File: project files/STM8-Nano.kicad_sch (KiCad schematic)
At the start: 29 parts, among them J1 RIGHT, J2 LEFT, J3 USB_C_Receptacle, J4 SWIM, SW1 RESET, SW2 VCC, U1 STM8F105K4, U2 CH340E, Y1 16MHZ

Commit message: added annotation
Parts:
- removed C7: 1uF, Capacitor_SMD:C_0603_1608Metric, symbol Device:C
- removed C8: 100nF, Capacitor_SMD:C_0603_1608Metric, symbol Device:C
- removed J3: USB_C_Receptacle, Connector_USB:USB_C_Receptacle_Palconn_UTC16-G, symbol Connector:USB_C_Receptacle
- removed L1: L, symbol Device:L
- added C9: 10uF, Capacitor_SMD:C_0603_1608Metric, symbol Device:C
- added J3: USB_C_Receptacle_USB2.0, Connector_USB:USB_C_Receptacle_Palconn_UTC16-G, symbol Connector:USB_C_Receptacle_USB2.0
- D2: value TX -> TX↓
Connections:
- net VDDA is gone; now on net VCC: U1.7 (VDDIO)
- net +5V: now also U2.7 (VCC)
- net GND: now also J4.3 (Pin_3), J3.A1 (GND), J3.A12 (GND), J3.B1 (GND), J3.B12 (GND); no longer J4.4 (Pin_4)
- net USB(+): now also J3.A6 (D+), J3.B6 (D+)
- net USB(-): now also J3.A7 (D-), J3.B7 (D-)
- net VCC: no longer U2.7 (VCC)
- net ~{RST}: now also J4.4 (Pin_4), C9.2; no longer J4.3 (Pin_3)
- net at R1.1: now also J3.B5 (CC2)
- net at R2.1: now also J3.A5 (CC1)
- net at U2.4 (~{RTS}): now also C9.1
- new net: J3.A4 (VBUS), J3.A9 (VBUS), J3.B4 (VBUS), J3.B9 (VBUS)
- no-connect marks 14 -> 5
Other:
- note added: "Arduino Nano pin functions: D1 | TX D0 | RX Reset GND D2 | Interrupt ~D3 | Interrupt D4 ~D5 ~D6 D7 D8 ~D9 ~D10 | SS ~D11 | MOSI ~D12 | MISO"
- note added: "Arduino Nano pin functions: Vin GND Reset +5V A7 | D21 A6 | D20 A5 | D19 | SCL A4 | D18 | SDA A3 | D17 A2 | D16 A1 | D15 A0 | D14 Aref +3.3V D13 | SCK"
- moved on the sheet: C3, C4, D1, D2, J1, J2, R3, R4, U2

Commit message: case change
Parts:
- removed R7: 0R, Resistor_SMD:R_0805_2012Metric, symbol Device:R
- C1, C3, C4, C5, C6, C9: footprint Capacitor_SMD:C_0603_1608Metric -> Capacitor_SMD:C_0402_1005Metric
- D1, D2, D3, D4: footprint LED_SMD:LED_0603_1608Metric -> LED_SMD:LED_0402_1005Metric
- R1, R2, R3, R4, R5, R6: footprint Resistor_SMD:R_0603_1608Metric_Pad0.98x0.95mm_HandSolder -> Resistor_SMD:R_0402_1005Metric

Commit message: up
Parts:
- SW2: footprint Jumper:SolderJumper-3_P2.0mm_Open_TrianglePad1.0x1.5mm_NumberLabels -> Button_Switch_SMD:SW_SPDT_PCM12
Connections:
- net VBUS: now reaches J3.A4 (VBUS), J3.A9 (VBUS), J3.B4 (VBUS), J3.B9 (VBUS)
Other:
- moved on the sheet: SW2
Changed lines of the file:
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@@
     (stroke (width 0) (type default) (color 0 0 0 0))
   )
-  (wire (pts (xy 17.78 123.19) (xy 17.78 120.65))
+  (wire (pts (xy 251.46 63.5) (xy 251.46 60.96))
     (stroke (width 0) (type default) (color 0 0 0 0))
   )
@@
     (stroke (width 0) (type default) (color 0 0 0 0))
   )
-  (wire (pts (xy 20.32 123.19) (xy 17.78 123.19))
+  (wire (pts (xy 254 63.5) (xy 251.46 63.5))
     (stroke (width 0) (type default) (color 0 0 0 0))
   )
@@
     (stroke (width 0) (type default) (color 0 0 0 0))
   )
-  (wire (pts (xy 38.1 125.73) (xy 38.1 120.65))
-    (stroke (width 0) (type default) (color 0 0 0 0))
-  )
-  (wire (pts (xy 30.48 120.65) (xy 33.02 120.65))
+  (wire (pts (xy 271.78 66.04) (xy 271.78 60.96))
+    (stroke (width 0) (type default) (color 0 0 0 0))
+  )
+  (wire (pts (xy 264.16 60.96) (xy 266.7 60.96))
     (stroke (width 0) (type default) (color 0 0 0 0))
   )
@@
     (stroke (width 0) (type default) (color 0 0 0 0))
   )
+  (wire (pts (xy 50.8 35.56) (xy 50.8 33.02))
+    (stroke (width 0) (type default) (color 0 0 0 0))
+  )
   (wire (pts (xy 154.94 54.61) (xy 160.02 54.61))
     (stroke (width 0) (type default) (color 0 0 0 0))
@@
     (stroke (width 0) (type default) (color 0 0 0 0))
   )
-  (wire (pts (xy 30.48 125.73) (xy 38.1 125.73))
+  (wire (pts (xy 264.16 66.04) (xy 271.78 66.04))
     (stroke (width 0) (type default) (color 0 0 0 0))
   )
@@
   )
   (wire (pts (xy 85.09 35.56) (xy 85.09 38.1))
+    (stroke (width 0) (type default) (color 0 0 0 0))
+  )
+  (wire (pts (xy 48.26 35.56) (xy 50.8 35.56))
     (stroke (width 0) (type default) (color 0 0 0 0))
   )
@@
   )
   (label "D1{slash}TX" (at 114.3 45.72 180)
+    (effects (font (size 1.27 1.27)) (justify right bottom))
+  )
+  (label "VIN" (at 55.88 142.24 180)
     (effects (font (size 1.27 1.27)) (justify right bottom))
   )
@@
     (pin "1")
     (pin "2")
+  )
+  (symbol (lib_id "power:+3.3V") (at 96.52 135.89 0) (unit 1)
+    (in_bom yes) (on_board yes) (fields_autoplaced)
+    (property "Reference" "#PWR0110" (id 0) (at 96.52 139.7 0)
+      (effects (font (size 1.27 1.27)) hide)
+    )
+    (property "Value" "+3.3V" (id 1) (at 96.52 130.81 0))
+    (property "Footprint" "" (id 2) (at 96.52 135.89 0)
+      (effects (font (size 1.27 1.27)) hide)
+    )
+    (property "Datasheet" "" (id 3) (at 96.52 135.89 0)
+      (effects (font (size 1.27 1.27)) hide)
+    )
+    (pin "1")
   )
   (symbol (lib_id "Connector_Generic:Conn_01x04") (at 274.32 29.21 0) (unit 1)
@@
     (pin "2")
   )
-  (symbol (lib_id "power:VCC") (at 17.78 120.65 0) (unit 1)
-    (in_bom yes) (on_board yes) (fields_autoplaced)
-    (property "Reference" "#PWR01" (id 0) (at 17.78 124.46 0)
-      (effects (font (size 1.27 1.27)) hide)
-    )
-    (property "Value" "VCC" (id 1) (at 17.78 115.57 0))
-    (property "Footprint" "" (id 2) (at 17.78 120.65 0)
-      (effects (font (size 1.27 1.27)) hide)
-    )
-    (property "Datasheet" "" (id 3) (at 17.78 120.65 0)
+  (symbol (lib_id "power:VCC") (at 251.46 60.96 0) (unit 1)
+    (in_bom yes) (on_board yes) (fields_autoplaced)
+    (property "Reference" "#PWR01" (id 0) (at 251.46 64.77 0)
+      (effects (font (size 1.27 1.27)) hide)
+    )
+    (property "Value" "VCC" (id 1) (at 251.46 55.88 0))
+    (property "Footprint" "" (id 2) (at 251.46 60.96 0)
+      (effects (font (size 1.27 1.27)) hide)
+    )
+    (property "Datasheet" "" (id 3) (at 251.46 60.96 0)
       (effects (font (size 1.27 1.27)) hide)
     )
@@
     (pin "2")
   )
-  (symbol (lib_id "power:+3.3V") (at 33.02 120.65 0) (unit 1)
-    (in_bom yes) (on_board yes) (fields_autoplaced)
-    (property "Reference" "#PWR07" (id 0) (at 33.02 124.46 0)
-      (effects (font (size 1.27 1.27)) hide)
-    )
-    (property "Value" "+3.3V" (id 1) (at 33.02 115.57 0))
-    (property "Footprint" "" (id 2) (at 33.02 120.65 0)
-      (effects (font (size 1.27 1.27)) hide)
-    )
-    (property "Datasheet" "" (id 3) (at 33.02 120.65 0)
+  (symbol (lib_id "power:+3.3V") (at 266.7 60.96 0) (unit 1)
+    (in_bom yes) (on_board yes) (fields_autoplaced)
+    (property "Reference" "#PWR07" (id 0) (at 266.7 64.77 0)
+      (effects (font (size 1.27 1.27)) hide)
+    )
+    (property "Value" "+3.3V" (id 1) (at 266.7 55.88 0))
+    (property "Footprint" "" (id 2) (at 266.7 60.96 0)
+      (effects (font (size 1.27 1.27)) hide)
+    )
+    (property "Datasheet" "" (id 3) (at 266.7 60.96 0)
       (effects (font (size 1.27 1.27)) hide)
     )
@@
     (pin "1")
   )
+  (symbol (lib_id "power:VBUS") (at 48.26 157.48 0) (unit 1)
+    (in_bom yes) (on_board yes) (fields_autoplaced)
+    (property "Reference" "#PWR0115" (id 0) (at 48.26 161.29 0)
+      (effects (font (size 1.27 1.27)) hide)
+    )
+    (property "Value" "VBUS" (id 1) (at 48.26 152.4 0))
+    (property "Footprint" "" (id 2) (at 48.26 157.48 0)
+      (effects (font (size 1.27 1.27)) hide)
+    )
+    (property "Datasheet" "" (id 3) (at 48.26 157.48 0)
+      (effects (font (size 1.27 1.27)) hide)
+    )
+    (pin "1")
+  )
   (symbol (lib_id "power:GND") (at 175.26 97.79 0) (unit 1)
     (in_bom yes) (on_board yes) (fields_autoplaced)
@@
     )
     (property "Datasheet" "" (id 3) (at 106.68 25.4 0)
+      (effects (font (size 1.27 1.27)) hide)
+    )
+    (pin "1")
+  )
+  (symbol (lib_id "power:+5V") (at 67.31 135.89 0) (unit 1)
+    (in_bom yes) (on_board yes) (fields_autoplaced)
+    (property "Reference" "#PWR0111" (id 0) (at 67.31 139.7 0)
+      (effects (font (size 1.27 1.27)) hide)
+    )
+    (property "Value" "+5V" (id 1) (at 67.31 130.81 0))
+    (property "Footprint" "" (id 2) (at 67.31 135.89 0)
+      (effects (font (size 1.27 1.27)) hide)
+    )
+    (property "Datasheet" "" (id 3) (at 67.31 135.89 0)
       (effects (font (size 1.27 1.27)) hide)
     )
@@
     (pin "1")
   )
-  (symbol (lib_id "power:+5V") (at 38.1 120.65 0) (unit 1)
-    (in_bom yes) (on_board yes) (fields_autoplaced)
-    (property "Reference" "#PWR06" (id 0) (at 38.1 124.46 0)
-      (effects (font (size 1.27 1.27)) hide)
-    )
-    (property "Value" "+5V" (id 1) (at 38.1 115.57 0))
-    (property "Footprint" "" (id 2) (at 38.1 120.65 0)
-      (effects (font (size 1.27 1.27)) hide)
-    )
-    (property "Datasheet" "" (id 3) (at 38.1 120.65 0)
+  (symbol (lib_id "power:+5V") (at 271.78 60.96 0) (unit 1)
+    (in_bom yes) (on_board yes) (fields_autoplaced)
+    (property "Reference" "#PWR06" (id 0) (at 271.78 64.77 0)
+      (effects (font (size 1.27 1.27)) hide)
+    )
+    (property "Value" "+5V" (id 1) (at 271.78 55.88 0))
+    (property "Footprint" "" (id 2) (at 271.78 60.96 0)
+      (effects (font (size 1.27 1.27)) hide)
+    )
+    (property "Datasheet" "" (id 3) (at 271.78 60.96 0)
+      (effects (font (size 1.27 1.27)) hide)
+    )
+    (pin "1")
+  )
+  (symbol (lib_id "power:VBUS") (at 50.8 33.02 0) (unit 1)
+    (in_bom yes) (on_board yes) (fields_autoplaced)
+    (property "Reference" "#PWR0109" (id 0) (at 50.8 36.83 0)
+      (effects (font (size 1.27 1.27)) hide)
+    )
+    (property "Value" "VBUS" (id 1) (at 50.8 27.94 0))
+    (property "Footprint" "" (id 2) (at 50.8 33.02 0)
+      (effects (font (size 1.27 1.27)) hide)
+    )
+    (property "Datasheet" "" (id 3) (at 50.8 33.02 0)
       (effects (font (size 1.27 1.27)) hide)
     )
@@
     (pin "2")
   )
-  (symbol (lib_id "Switch:SW_Push_SPDT") (at 25.4 123.19 0) (unit 1)
-    (in_bom yes) (on_board yes) (fields_autoplaced)
-    (property "Reference" "SW2" (id 0) (at 25.4 115.57 0))
-    (property "Value" "VCC" (id 1) (at 25.4 118.11 0))
-    (property "Footprint" "Jumper:SolderJumper-3_P2.0mm_Open_TrianglePad1.0x1.5mm_NumberLabels" (id 2) (at 25.4 123.19 0)
-      (effects (font (size 1.27 1.27)) hide)
-    )
-    (property "Datasheet" "~" (id 3) (at 25.4 123.19 0)
+  (symbol (lib_id "Switch:SW_Push_SPDT") (at 259.08 63.5 0) (unit 1)
+    (in_bom yes) (on_board yes) (fields_autoplaced)
+    (property "Reference" "SW2" (id 0) (at 259.08 55.88 0))
+    (property "Value" "VCC" (id 1) (at 259.08 58.42 0))
+    (property "Footprint" "Button_Switch_SMD:SW_SPDT_PCM12" (id 2) (at 259.08 63.5 0)
+      (effects (font (size 1.27 1.27)) hide)
+    )
+    (property "Datasheet" "~" (id 3) (at 259.08 63.5 0)
       (effects (font (size 1.27 1.27)) hide)
     )
@@
       (reference "#PWR0108") (unit 1) (value "VCC") (footprint "")
     )
+    (path "/eb2c21a5-a0b7-44ce-9b89-202ae5311275"
+      (reference "#PWR0109") (unit 1) (value "VBUS") (footprint "")
+    )
+    (path "/177d57ad-c7e9-4634-ac17-80ec90208662"
+      (reference "#PWR0110") (unit 1) (value "+3.3V") (footprint "")
+    )
+    (path "/a9001576-5569-431d-9cb0-cf736b52953b"
+      (reference "#PWR0111") (unit 1) (value "+5V") (footprint "")
+    )
     (path "/08fe6a42-f88e-473c-9240-97ab0a243355"
       (reference "#PWR0112") (unit 1) (value "GND") (footprint "")
@@
       (reference "#PWR0114") (unit 1) (value "+5V") (footprint "")
     )
+    (path "/9989b91c-5095-4ba2-b2e0-afbf24ce0e2a"
+      (reference "#PWR0115") (unit 1) (value "VBUS") (footprint "")
+    )
     (path "/b8b0b547-dc08-4bb4-b7a3-b575872bca38"
       (reference "C1") (unit 1) (value "100nF") (footprint "Capacitor_SMD:C_0402_1005Metric")
@@
     )
     (path "/f8b6bb44-7ca1-453d-9867-81548ee679a2"
-      (reference "SW2") (unit 1) (value "VCC") (footprint "Jumper:SolderJumper-3_P2.0mm_Open_TrianglePad1.0x1.5mm_NumberLabels")
+      (reference "SW2") (unit 1) (value "VCC") (footprint "Button_Switch_SMD:SW_SPDT_PCM12")
     )
     (path "/1fb531c0-3a6f-47fd-bb65-8aa83b1751ae"

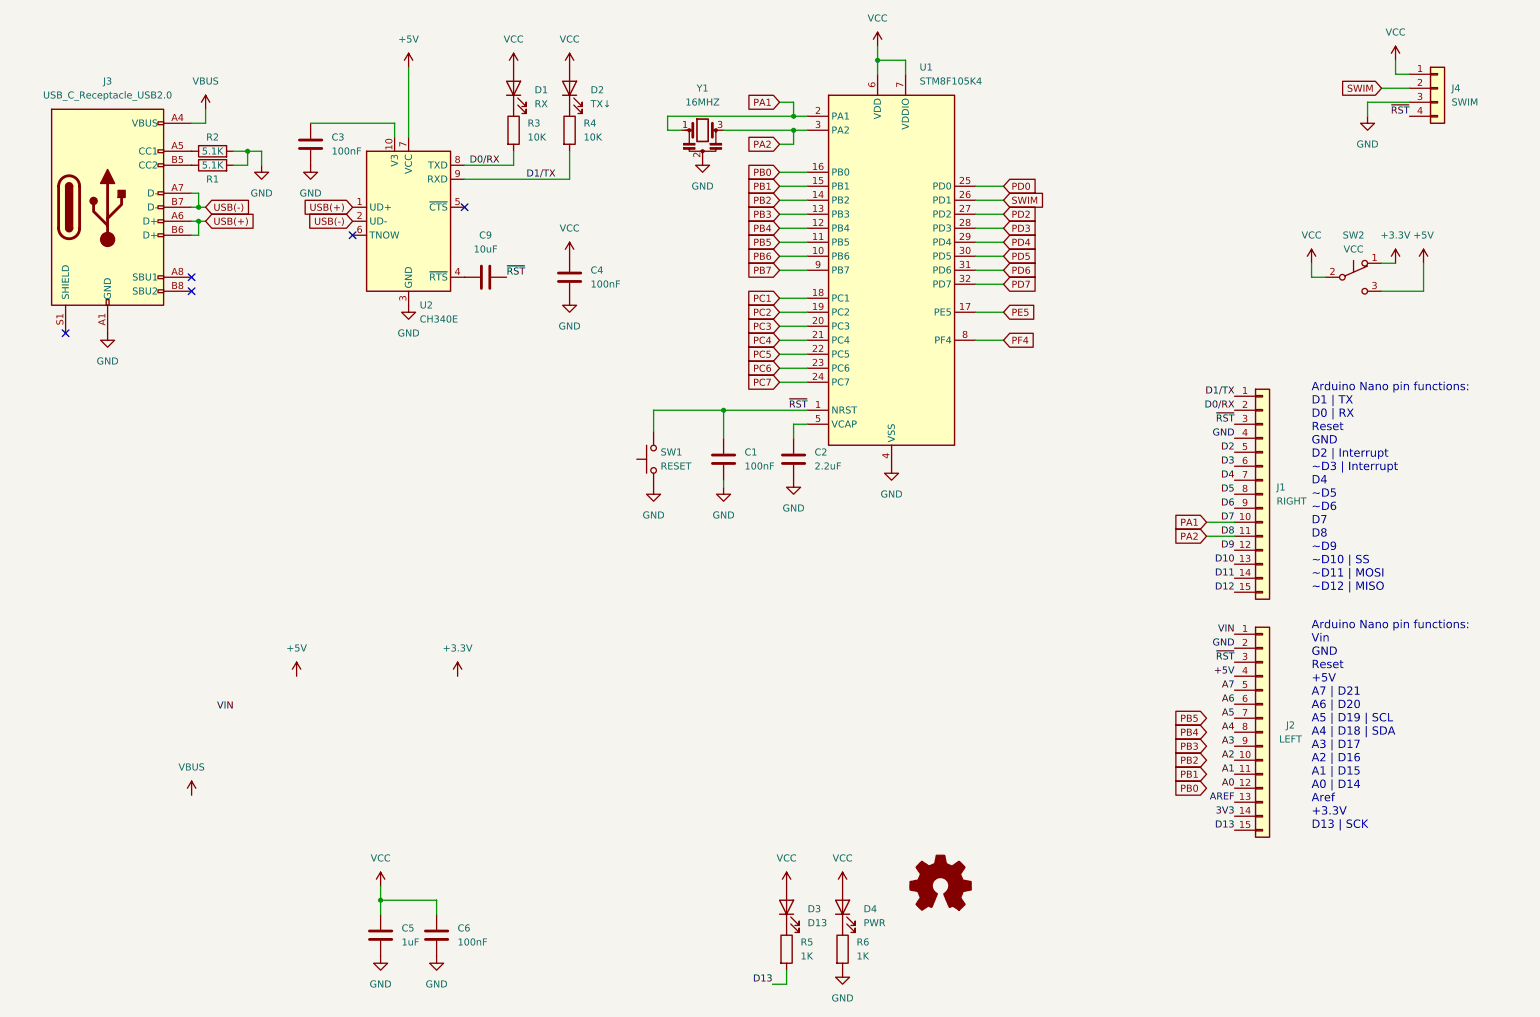
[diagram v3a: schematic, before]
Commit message: LED moved
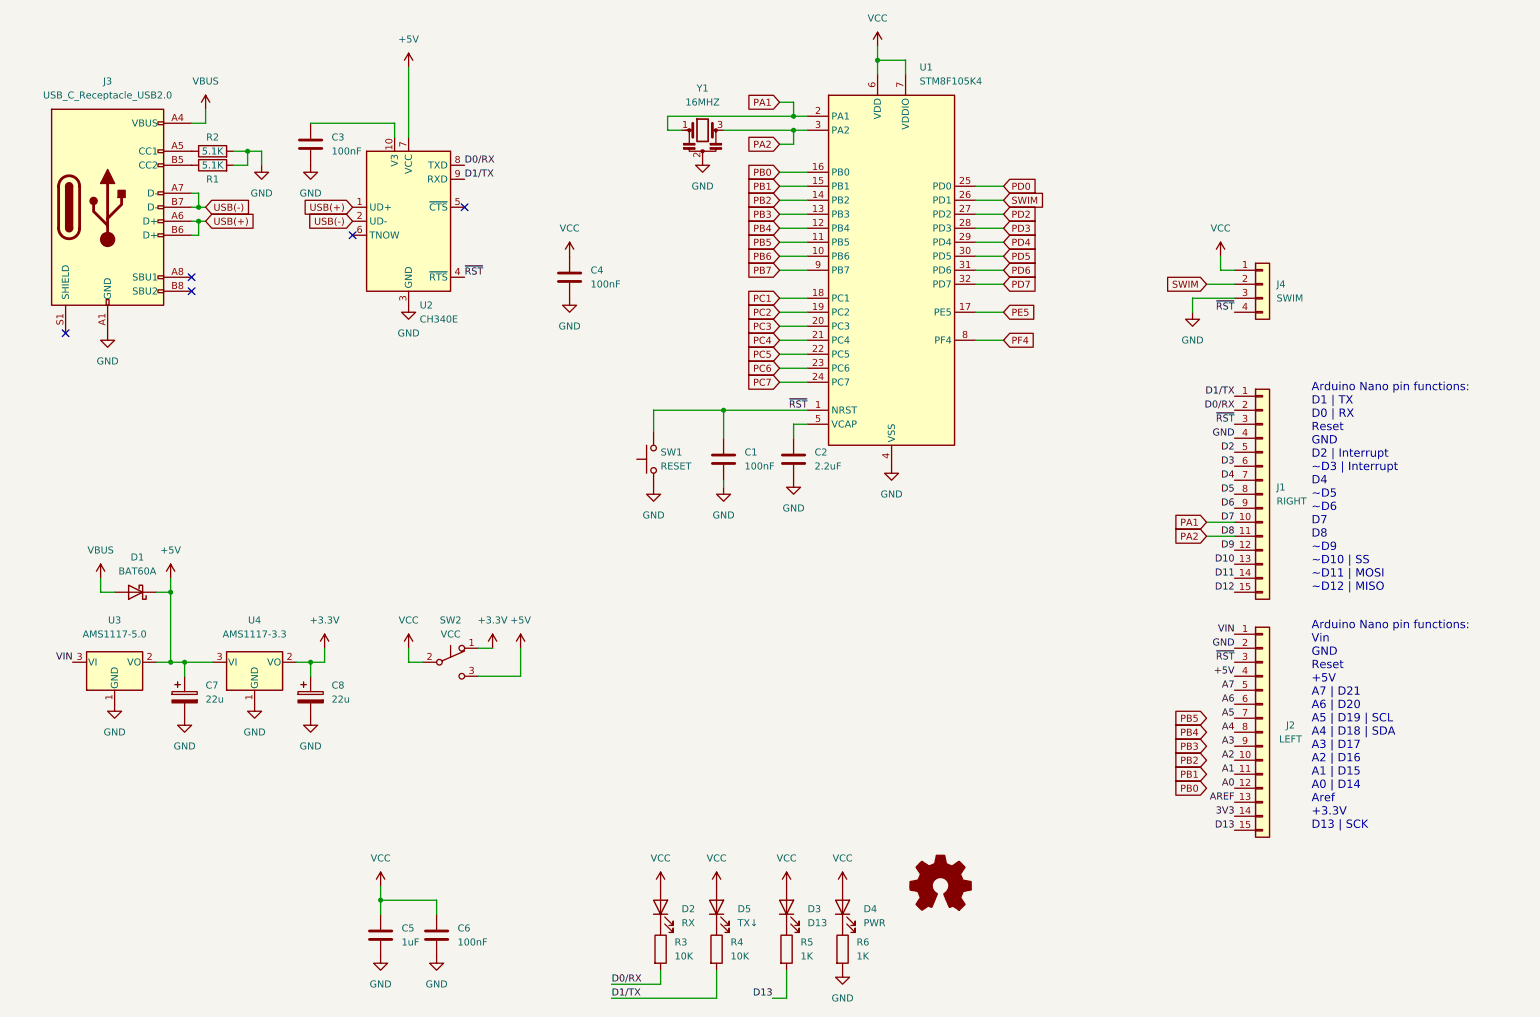
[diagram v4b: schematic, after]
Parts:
- removed C9: 10uF, Capacitor_SMD:C_0402_1005Metric, symbol Device:C
- removed D1: RX, LED_SMD:LED_0402_1005Metric, symbol Device:LED
- added C7, C8: 22u, symbol Device:C_Polarized
- added D1: BAT60A, Diode_SMD:D_SOD-323, symbol Diode:BAT60A
- added D5: TX↓, LED_SMD:LED_0402_1005Metric, symbol Device:LED
- added U3: AMS1117-5.0, Package_TO_SOT_SMD:SOT-223-3_TabPin2, symbol Regulator_Linear:AMS1117-5.0
- added U4: AMS1117-3.3, Package_TO_SOT_SMD:SOT-223-3_TabPin2, symbol Regulator_Linear:AMS1117-3.3
- D2: value TX↓ -> RX
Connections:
- net +3.3V: now also C8.1, U4.2 (VO)
- net +5V: now also C7.1, D1.1 (K), U3.2 (VO), U4.3 (VI)
- net GND: now also C7.2, C8.2, U3.1 (GND), U4.1 (GND)
- net VBUS: now also D1.2 (A)
- net VCC: now also D5.2 (A)
- net VIN: now also U3.3 (VI)
- net ~{RST}: now also U2.4 (~{RTS})
- net at R3.1: now also D2.1 (K)
- net at R4.1: now also D5.1 (K); no longer D2.1 (K)
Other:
- moved on the sheet: J4, SW2
